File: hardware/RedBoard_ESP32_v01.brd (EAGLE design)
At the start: 68.6 x 58.4 mm, 206 parts, among them J1 5.5x2.1mm Barrel, J13 QWIIC_RIGHT_ANGLE, J15 MICRO-SD-PUSH-PUSH-EXT-PIN, J2 USB C, J3 USB_SOLDER_PADS, J5 M10NO_SILK, Q1 MBT3904DW1T1, Q11 20V/4.2A/52mΩ/1.4W, Q13 20V/4.2A/52mΩ/1.4W, Q3 20V/4.2A/52mΩ/1.4W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

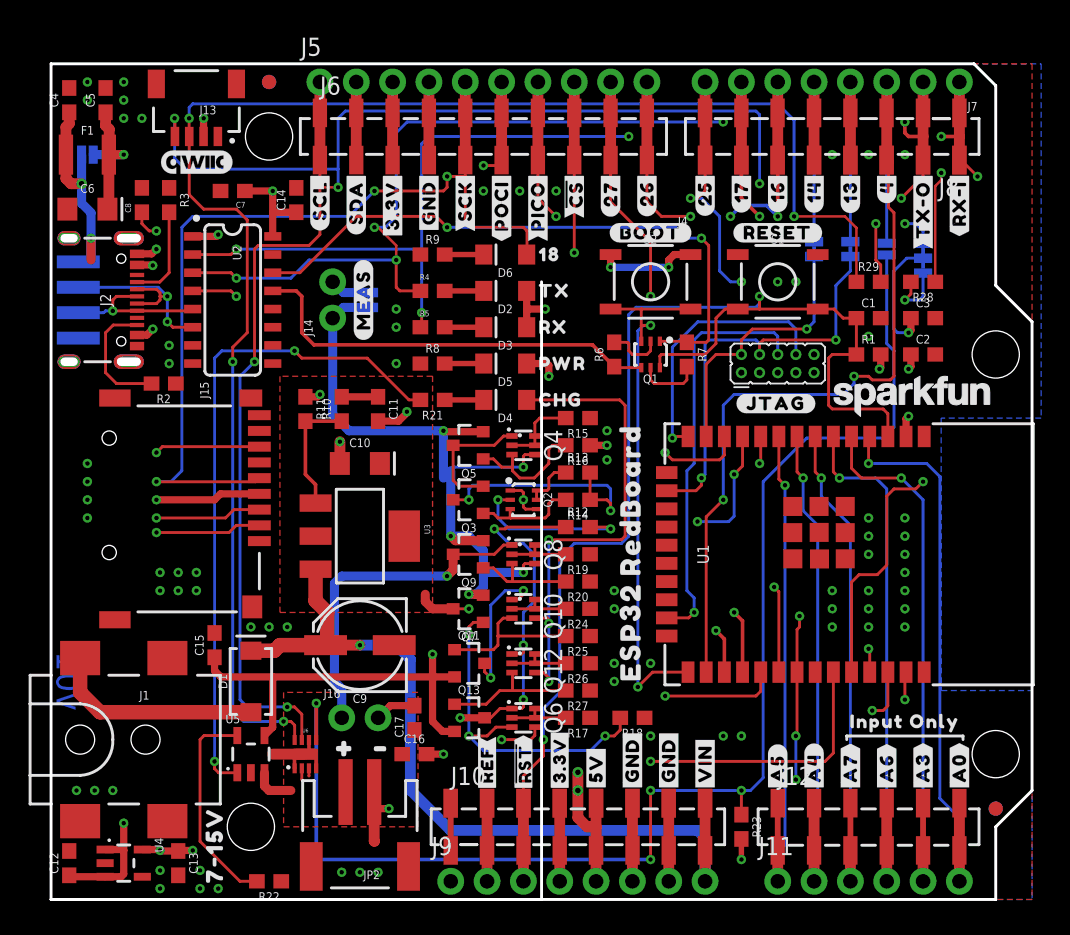
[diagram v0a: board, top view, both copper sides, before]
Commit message: Added Test Point per Eric Orosel request.
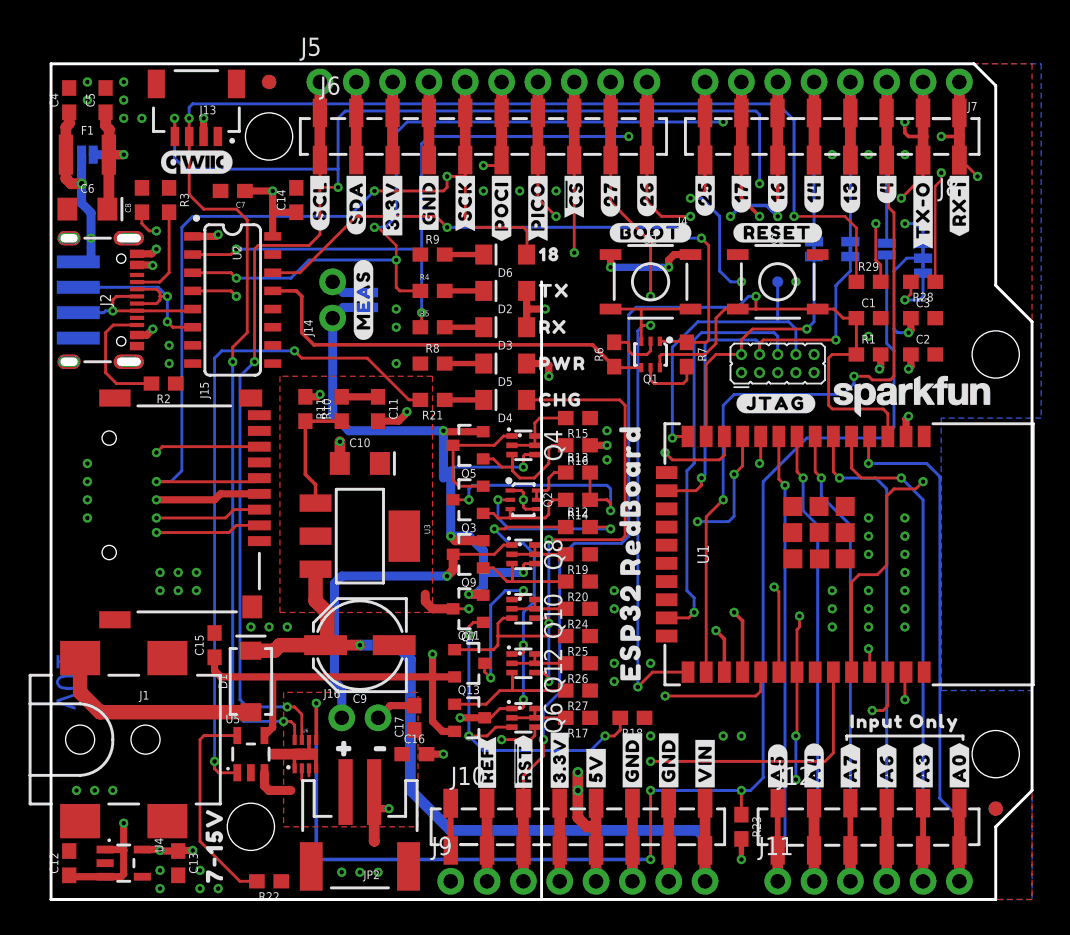
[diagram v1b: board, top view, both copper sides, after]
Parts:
- added TP1: TEST-POINT3, SparkFun-Connectors:PAD.03X.03
- added U$95: (no value), output-ESP32:TP1321868
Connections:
- net ESP32_GPIO12_TDI: now also TP1.1
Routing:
- net ESP32_GPIO12_TDI: track 18.9 -> 21.6 mm
- net VUSB: track 29.9 -> 28.4 mm
- net ESP32_EN: track 86.5 -> 86.0 mm
- net ESP32_RXD0: track 115.3 -> 114.7 mm
- net 5V_CHG: track 72.4 -> 71.9 mm
- net GND: vias 80 -> 79

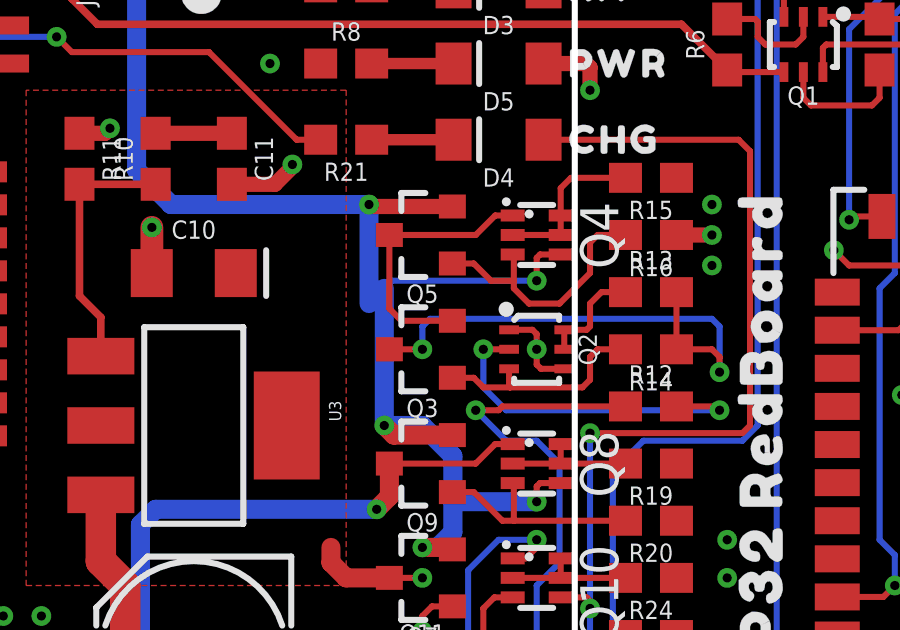
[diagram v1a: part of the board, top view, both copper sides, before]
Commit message: Fixed trace on bottom side, regenerated panel file.
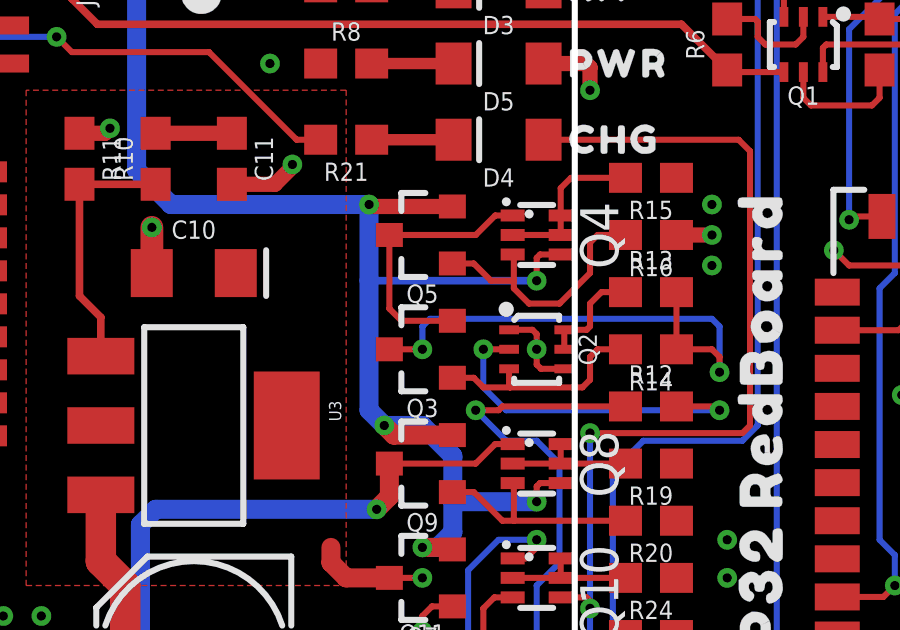
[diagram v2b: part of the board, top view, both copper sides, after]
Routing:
- net 5V_MEAS: track 65.2 -> 64.6 mm
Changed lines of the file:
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@@
 <drawing>
 <settings>
-<setting alwaysvectorfont="yes"/>
+<setting alwaysvectorfont="no"/>
 <setting keepoldvectorfont="yes"/>
 <setting verticaltext="up"/>
@@
 <layers>
 <layer number="1" name="Top" color="4" fill="1" visible="yes" active="yes"/>
-<layer number="2" name="Route2" color="24" fill="1" visible="yes" active="yes"/>
+<layer number="2" name="Route2" color="24" fill="1" visible="no" active="yes"/>
 <layer number="15" name="Route15" color="23" fill="1" visible="no" active="yes"/>
 <layer number="16" name="Bottom" color="1" fill="1" visible="yes" active="yes"/>
@@
 <wire x1="28.26" y1="25.08" x2="27.94" y2="25.4" width="0.635" layer="1"/>
 <via x="27.94" y="25.4" extent="1-16" drill="0.3048"/>
-<wire x1="27.94" y1="25.4" x2="27.94" y2="29.972" width="0.635" layer="16"/>
+<wire x1="27.94" y1="25.4" x2="27.432" y2="25.908" width="0.635" layer="16"/>
+<wire x1="27.432" y1="30.226" x2="27.432" y2="25.908" width="0.635" layer="16"/>
 <via x="27.432" y="32.766" extent="1-16" drill="0.3048"/>
-<wire x1="27.432" y1="29.464" x2="27.432" y2="32.766" width="0.635" layer="16"/>
+<wire x1="27.432" y1="30.226" x2="27.432" y2="32.766" width="0.635" layer="16"/>
 <wire x1="19.685" y1="40.64" x2="19.685" y2="33.909" width="0.635" layer="16"/>
 <wire x1="19.685" y1="33.909" x2="20.828" y2="32.766" width="0.635" layer="16"/>
@@
 <wire x1="33.02" y1="30.988" x2="33.02" y2="30.226" width="0.2032" layer="1"/>
 <via x="33.02" y="30.226" extent="1-16" drill="0.3048"/>
-<wire x1="33.02" y1="30.226" x2="28.194" y2="30.226" width="0.2032" layer="16"/>
-<wire x1="28.194" y1="30.226" x2="27.94" y2="29.972" width="0.2032" layer="16"/>
-<wire x1="27.94" y1="29.972" x2="27.432" y2="29.464" width="0.2032" layer="16"/>
 <wire x1="33.82" y1="23.48" x2="33.132" y2="23.48" width="0.2032" layer="1"/>
 <wire x1="33.132" y1="23.48" x2="33.02" y2="23.368" width="0.2032" layer="1"/>
@@
 <wire x1="30.21" y1="32.7" x2="27.498" y2="32.7" width="0.508" layer="1"/>
 <wire x1="27.498" y1="32.7" x2="27.432" y2="32.766" width="0.508" layer="1"/>
+<wire x1="33.02" y1="30.226" x2="27.432" y2="30.226" width="0.254" layer="16"/>
 </signal>
 <signal name="N$18">

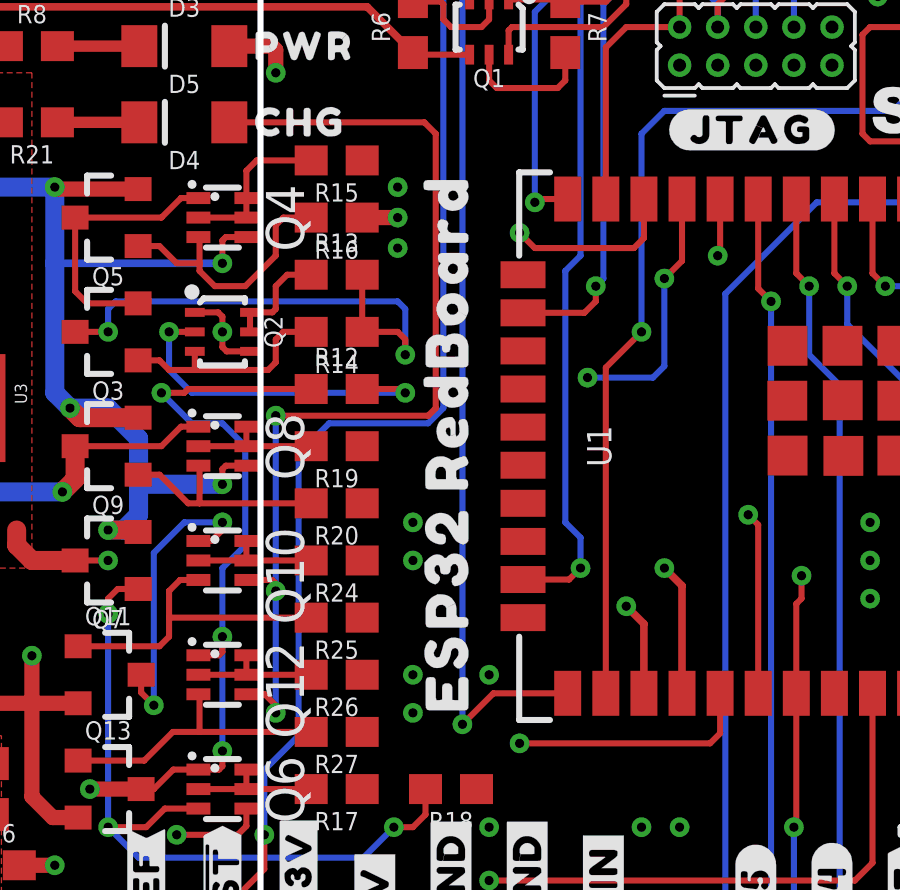
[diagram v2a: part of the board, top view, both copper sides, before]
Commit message: Changed labels as suggested by Chris; updated production files.
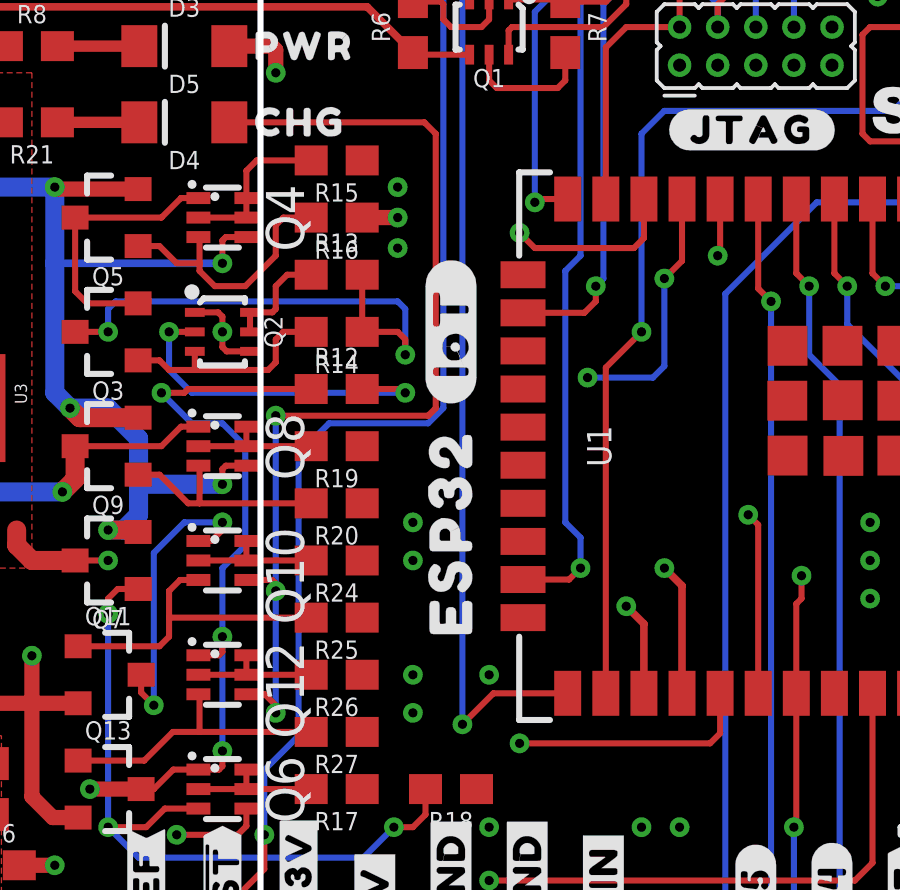
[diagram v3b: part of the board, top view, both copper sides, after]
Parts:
- added U$100: (no value), output-ESP32:#IOT#132321869
- added U$98: (no value), SparkFun-Aesthetics:REDBOARD_LOGO
- added U$99: (no value), output-ESP32:THE_USA32321858
- U$47: device output-ESP32:REDBOARD321856 -> output-ESP32:#IOT#132321874
- U$93: device output-ESP32:ESP32_REDBOARD321857 -> output-ESP32:ESP32321856
- U$94: device output-ESP32:MADE_IN_THE_USA321857 -> output-ESP32:MADE_IN32321857
- moved U$47 12.6 mm to (27.9, 21.5), flipped to the bottom, turned to 0 degrees
- moved U$93 8.63 mm to (38.1, 21.5)
- moved LOGO6 3.81 mm to (34.3, 38.1)
- moved U$48 2.54 mm to (40.6, 16.8)
- moved U$94 2.54 mm to (34.3, 16.5)
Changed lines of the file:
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@@
 <setting verticaltext="up"/>
 </settings>
-<grid distance="0.01" unitdist="inch" unit="inch" style="lines" multiple="1" display="yes" altdistance="0.005" altunitdist="inch" altunit="inch"/>
+<grid distance="0.05" unitdist="inch" unit="inch" style="lines" multiple="1" display="yes" altdistance="0.005" altunitdist="inch" altunit="inch"/>
 <layers>
 <layer number="1" name="Top" color="4" fill="1" visible="yes" active="yes"/>
-<layer number="2" name="Route2" color="24" fill="1" visible="no" active="yes"/>
-<layer number="15" name="Route15" color="23" fill="1" visible="no" active="yes"/>
+<layer number="2" name="Route2" color="24" fill="1" visible="yes" active="yes"/>
+<layer number="15" name="Route15" color="23" fill="1" visible="yes" active="yes"/>
 <layer number="16" name="Bottom" color="1" fill="1" visible="yes" active="yes"/>
 <layer number="17" name="Pads" color="2" fill="1" visible="yes" active="yes"/>
@@
 <layer number="23" name="tOrigins" color="15" fill="1" visible="yes" active="yes"/>
 <layer number="24" name="bOrigins" color="15" fill="1" visible="yes" active="yes"/>
-<layer number="25" name="tNames" color="7" fill="1" visible="no" active="yes"/>
-<layer number="26" name="bNames" color="7" fill="1" visible="no" active="yes"/>
-<layer number="27" name="tValues" color="7" fill="1" visible="no" active="yes"/>
-<layer number="28" name="bValues" color="7" fill="1" visible="no" active="yes"/>
-<layer number="29" name="tStop" color="7" fill="3" visible="no" active="yes"/>
-<layer number="30" name="bStop" color="7" fill="6" visible="no" active="yes"/>
-<layer number="31" name="tCream" color="7" fill="4" visible="no" active="yes"/>
-<layer number="32" name="bCream" color="7" fill="5" visible="no" active="yes"/>
-<layer number="33" name="tFinish" color="6" fill="3" visible="no" active="yes"/>
-<layer number="34" name="bFinish" color="6" fill="6" visible="no" active="yes"/>
-<layer number="35" name="tGlue" color="7" fill="4" visible="no" active="yes"/>
-<layer number="36" name="bGlue" color="7" fill="5" visible="no" active="yes"/>
-<layer number="37" name="tTest" color="7" fill="1" visible="no" active="yes"/>
-<layer number="38" name="bTest" color="7" fill="1" visible="no" active="yes"/>
-<layer number="39" name="tKeepout" color="4" fill="11" visible="no" active="yes"/>
-<layer number="40" name="bKeepout" color="1" fill="11" visible="no" active="yes"/>
-<layer number="41" name="tRestrict" color="4" fill="10" visible="no" active="yes"/>
-<layer number="42" name="bRestrict" color="1" fill="10" visible="no" active="yes"/>
-<layer number="43" name="vRestrict" color="2" fill="10" visible="no" active="yes"/>
-<layer number="44" name="Drills" color="7" fill="1" visible="no" active="yes"/>
+<layer number="25" name="tNames" color="7" fill="1" visible="yes" active="yes"/>
+<layer number="26" name="bNames" color="7" fill="1" visible="yes" active="yes"/>
+<layer number="27" name="tValues" color="7" fill="1" visible="yes" active="yes"/>
+<layer number="28" name="bValues" color="7" fill="1" visible="yes" active="yes"/>
+<layer number="29" name="tStop" color="7" fill="3" visible="yes" active="yes"/>
+<layer number="30" name="bStop" color="7" fill="6" visible="yes" active="yes"/>
+<layer number="31" name="tCream" color="7" fill="4" visible="yes" active="yes"/>
+<layer number="32" name="bCream" color="7" fill="5" visible="yes" active="yes"/>
+<layer number="33" name="tFinish" color="6" fill="3" visible="yes" active="yes"/>
+<layer number="34" name="bFinish" color="6" fill="6" visible="yes" active="yes"/>
+<layer number="35" name="tGlue" color="7" fill="4" visible="yes" active="yes"/>
+<layer number="36" name="bGlue" color="7" fill="5" visible="yes" active="yes"/>
+<layer number="37" name="tTest" color="7" fill="1" visible="yes" active="yes"/>
+<layer number="38" name="bTest" color="7" fill="1" visible="yes" active="yes"/>
+<layer number="39" name="tKeepout" color="4" fill="11" visible="yes" active="yes"/>
+<layer number="40" name="bKeepout" color="1" fill="11" visible="yes" active="yes"/>
+<layer number="41" name="tRestrict" color="4" fill="10" visible="yes" active="yes"/>
+<layer number="42" name="bRestrict" color="1" fill="10" visible="yes" active="yes"/>
+<layer number="43" name="vRestrict" color="2" fill="10" visible="yes" active="yes"/>
+<layer number="44" name="Drills" color="7" fill="1" visible="yes" active="yes"/>
 <layer number="45" name="Holes" color="7" fill="1" visible="yes" active="yes"/>
-<layer number="46" name="Milling" color="3" fill="1" visible="no" active="yes"/>
-<layer number="47" name="Measures" color="7" fill="1" visible="no" active="yes"/>
-<layer number="48" name="Document" color="7" fill="1" visible="no" active="yes"/>
-<layer number="49" name="Reference" color="7" fill="1" visible="no" active="yes"/>
-<layer number="50" name="dxf" color="7" fill="1" visible="no" active="yes"/>
+<layer number="46" name="Milling" color="3" fill="1" visible="yes" active="yes"/>
+<layer number="47" name="Measures" color="7" fill="1" visible="yes" active="yes"/>
+<layer number="48" name="Document" color="7" fill="1" visible="yes" active="yes"/>
+<layer number="49" name="Reference" color="7" fill="1" visible="yes" active="yes"/>
+<layer number="50" name="dxf" color="7" fill="1" visible="yes" active="yes"/>
 <layer number="51" name="tDocu" color="6" fill="1" visible="yes" active="yes"/>
-<layer number="52" name="bDocu" color="7" fill="1" visible="no" active="yes"/>
+<layer number="52" name="bDocu" color="7" fill="1" visible="yes" active="yes"/>
 <layer number="91" name="Nets" color="2" fill="1" visible="no" active="no"/>
 <layer number="92" name="Busses" color="1" fill="1" visible="no" active="no"/>
@@
 <element name="U$45" library="output-ESP32" package="#BATT#1848" value="" x="21.59" y="14.859" smashed="yes" rot="MR0"/>
 <element name="U$46" library="output-ESP32" package="#JTAG#1847" value="" x="50.673" y="34.671" smashed="yes" rot="MR0"/>
-<element name="U$48" library="output-ESP32" package="ESP321855" value="" x="40.513" y="14.224" smashed="yes" rot="R90"/>
+<element name="U$48" library="output-ESP32" package="ESP321855" value="" x="40.64" y="16.764" smashed="yes" rot="R90"/>
 <element name="U$49" library="output-ESP32" package="7#15V32321861" value="" x="11.43" y="3.81" smashed="yes" rot="R90"/>
 <element name="U$50" library="output-ESP32" package="#39#A3#321862" value="" x="60.96" y="1.778" smashed="yes" rot="MR90"/>
@@
 <element name="U$91" library="output-ESP32" package="#TMS#1854" value="" x="53.34" y="44.45" smashed="yes" rot="MR90"/>
 <element name="U$92" library="output-ESP32" package="#TCK#1853" value="" x="55.88" y="44.45" smashed="yes" rot="MR90"/>
-<element name="LOGO6" library="SparkFun-Aesthetics" package="SFE_LOGO_NAME_FLAME_.2" value="SFE_LOGO_NAME_FLAME.2_INCH" x="34.29" y="34.29" smashed="yes" rot="MR0"/>
-<element name="U$94" library="output-ESP32" package="MADE_IN_THE_USA321857" value="" x="34.29" y="19.05" smashed="yes" rot="MR0"/>
-<element name="U$93" library="output-ESP32" package="ESP32_REDBOARD321857" value="" x="34.29" y="29.21" smashed="yes" rot="MR0"/>
-<element name="U$47" library="output-ESP32" package="REDBOARD321856" value="" x="40.513" y="21.59" smashed="yes" rot="R90"/>
+<element name="LOGO6" library="SparkFun-Aesthetics" package="SFE_LOGO_NAME_FLAME_.2" value="SFE_LOGO_NAME_FLAME.2_INCH" x="34.29" y="38.1" smashed="yes" rot="MR0"/>
 <element name="U$96" library="output-ESP32" package="INPUT_ONLY321867" value="" x="59.69" y="12.446" smashed="yes"/>
 <element name="U$97" library="output-ESP32" package="INPUT_ONLY321867" value="" x="59.69" y="10.922" smashed="yes" rot="MR0"/>
@@
 <element name="TP1" library="SparkFun-Connectors" package="PAD.03X.03" value="TEST-POINT3" x="50.8" y="43.18" smashed="yes" rot="MR0"/>
 <element name="U$95" library="output-ESP32" package="TP1321868" value="" x="50.8" y="45.212" smashed="yes" rot="MR90"/>
+<element name="U$98" library="SparkFun-Aesthetics" package="REDBOARD_LOGO" value="" x="45.72" y="22.86" smashed="yes" rot="MR0"/>
+<element name="U$100" library="output-ESP32" package="#IOT#132321869" value="" x="40.64" y="27.94" smashed="yes" rot="R90"/>
+<element name="U$93" library="output-ESP32" package="ESP32321856" value="" x="38.1" y="21.463" smashed="yes" rot="MR0"/>
+<element name="U$47" library="output-ESP32" package="#IOT#132321874" value="" x="27.94" y="21.463" smashed="yes" rot="MR0"/>
+<element name="U$94" library="output-ESP32" package="MADE_IN32321857" value="" x="34.29" y="16.51" smashed="yes" rot="MR0"/>
+<element name="U$99" library="output-ESP32" package="THE_USA32321858" value="" x="34.29" y="13.97" smashed="yes" rot="MR0"/>
 </elements>
 <signals>
